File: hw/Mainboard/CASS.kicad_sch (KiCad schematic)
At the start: 16 parts, among them J5 CASS A, J6 CASS B, Q1 AO3401A, Q3 AO3401A

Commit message: Document schematics
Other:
- note added: "Solder jumpers allow cassette ports A/B to be configured as device 1 or 2. This is to support the original chicklet PETs where the internal cassette port is device 1 for use with the built-in Datasette. From schematics, MOTOR voltage appears to be 6.1V @ 350ma max per port. Datasettes uses a centrifugal speed governor, so voltage is not critical. +5V is rated 100ma per Datasette port. LED provide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"
- note removed: "+5V is 100ma per Datasette MOTOR is 6.1V @ 350ma max (older C2Ns draw more) SWITCH: 5v = Not pressed, Gnd = Pressed MOTOR: 5v = Off, Gnd = On (PIA1, pin 19)"
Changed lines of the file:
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@@
     (stroke (width 0) (type default) (color 0 0 0 0))
   )
-  (text "+5V is 100ma per Datasette\nMOTOR is 6.1V @ 350ma max (older C2Ns draw more)\n\nSWITCH: 5v = Not pressed, Gnd = Pressed\nMOTOR: 5v = Off, Gnd = On (PIA1, pin 19)\n"
-    (at 190.5 46.99 0)
+  (text "Solder jumpers allow cassette ports A/B to be configured as device 1 or 2.\nThis is to support the original chicklet PETs where the internal cassette\nport is device 1 for use with the built-in Datasette.\n\nFrom schematics, MOTOR voltage appears to be 6.1V @ 350ma max per port.\nDatasettes uses a centrifugal speed governor, so voltage is not critical.\n+5V is rated 100ma per Datasette port.\n\nLED provides an ~2V drop.  This accounts for the difference between the\n5V CMOS logic and the +6V input, causing the P-Channel MOSFET to turn off\ncompletely when ~{MOTOR} is high.  It also avoids over-voltaging the PIA.\n"
+    (at 190.5 57.15 0)
     (effects (font (size 1.27 1.27)) (justify left bottom))
   )
@@
   )
   (symbol (lib_id "power:+6V") (at 214.63 114.3 0) (unit 1)
-    (in_bom yes) (on_board yes) (fields_autoplaced)
+    (in_bom yes) (on_board yes)
     (property "Reference" "#PWR0125" (id 0) (at 214.63 118.11 0)
       (effects (font (size 1.27 1.27)) hide)
     )
-    (property "Value" "+6V" (id 1) (at 214.63 108.585 0))
+    (property "Value" "+6V" (id 1) (at 214.63 109.855 0))
     (property "Footprint" "" (id 2) (at 214.63 114.3 0)
       (effects (font (size 1.27 1.27)) hide)
@@
   )
   (symbol (lib_id "power:+6V") (at 214.63 82.55 0) (unit 1)
-    (in_bom yes) (on_board yes) (fields_autoplaced)
+    (in_bom yes) (on_board yes)
     (property "Reference" "#PWR0135" (id 0) (at 214.63 86.36 0)
       (effects (font (size 1.27 1.27)) hide)
     )
-    (property "Value" "+6V" (id 1) (at 214.63 76.835 0))
+    (property "Value" "+6V" (id 1) (at 214.63 78.105 0))
     (property "Footprint" "" (id 2) (at 214.63 82.55 0)
       (effects (font (size 1.27 1.27)) hide)

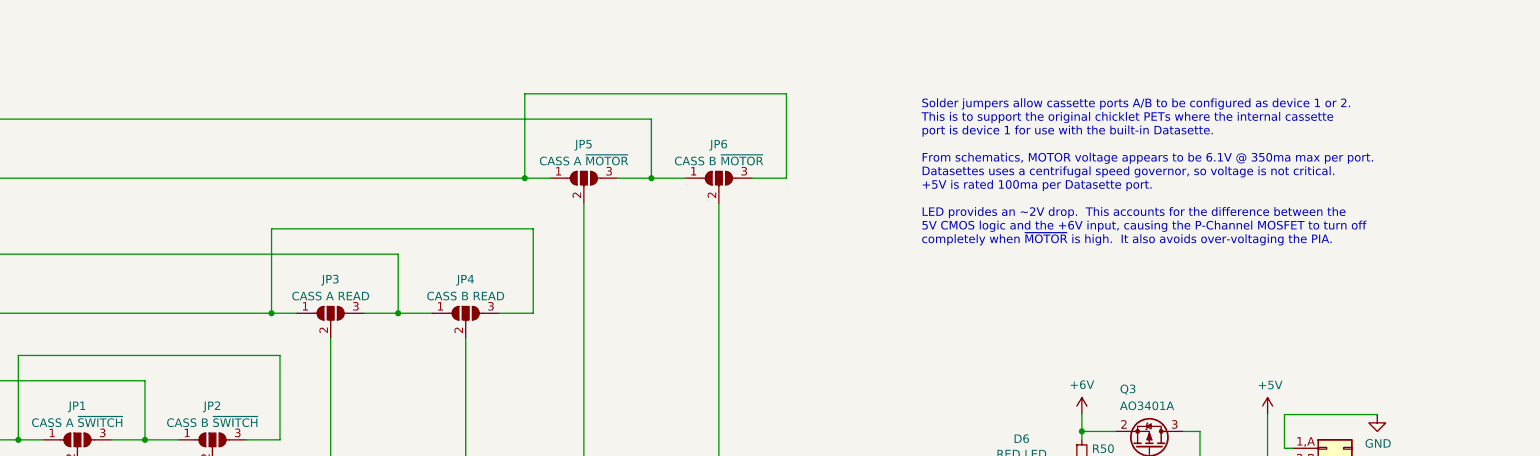
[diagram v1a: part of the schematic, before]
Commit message: hw: more schematic comments / cleanup
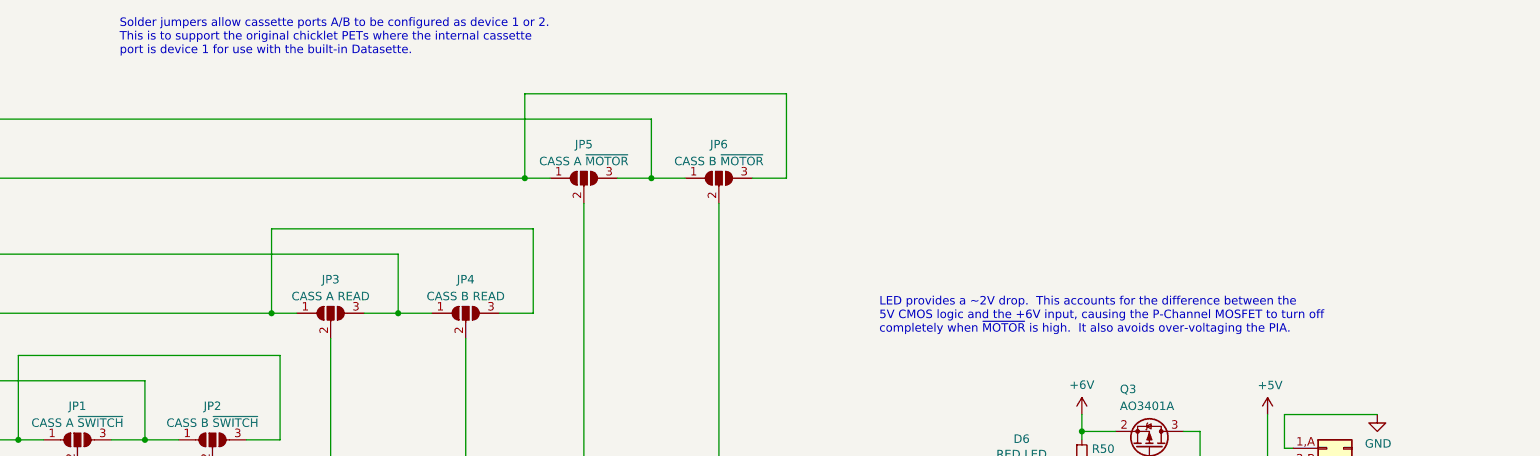
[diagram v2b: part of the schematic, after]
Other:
- note added: "LED provides a ~2V drop. This accounts for the difference between the 5V CMOS logic and the +6V input, causing the P-Channel MOSFET to turn off completely when ~{MOTOR} is high. It also avoids over-voltaging the PIA."
- note added: "Solder jumpers allow cassette ports A/B to be configured as device 1 or 2. This is to support the original chicklet PETs where the internal cassette port is device 1 for use with the built-in Datasette."
- note removed: "Solder jumpers allow cassette ports A/B to be configured as device 1 or 2. This is to support the original chicklet PETs where the internal cassette port is device 1 for use with the built-in Datasette. From schematics, MOTOR voltage appears to be 6.1V @ 350ma max per port. Datasettes uses a centrifugal speed governor, so voltage is not critical. +5V is rated 100ma per Datasette port. LED provide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"
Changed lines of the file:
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@@
     (stroke (width 0) (type default) (color 0 0 0 0))
   )
-  (text "Solder jumpers allow cassette ports A/B to be configured as device 1 or 2.\nThis is to support the original chicklet PETs where the internal cassette\nport is device 1 for use with the built-in Datasette.\n\nFrom schematics, MOTOR voltage appears to be 6.1V @ 350ma max per port.\nDatasettes uses a centrifugal speed governor, so voltage is not critical.\n+5V is rated 100ma per Datasette port.\n\nLED provides an ~2V drop.  This accounts for the difference between the\n5V CMOS logic and the +6V input, causing the P-Channel MOSFET to turn off\ncompletely when ~{MOTOR} is high.  It also avoids over-voltaging the PIA.\n"
-    (at 190.5 57.15 0)
+  (text "Solder jumpers allow cassette ports A/B to be configured as device 1 or 2.\nThis is to support the original chicklet PETs where the internal cassette\nport is device 1 for use with the built-in Datasette.\n"
+    (at 69.85 28.575 0)
     (effects (font (size 1.27 1.27)) (justify left bottom))
   )
+  (text "LED provides a ~2V drop.  This accounts for the difference between the\n5V CMOS logic and the +6V input, causing the P-Channel MOSFET to turn off\ncompletely when ~{MOTOR} is high.  It also avoids over-voltaging the PIA."
+    (at 184.15 70.485 0)
+    (effects (font (size 1.27 1.27)) (justify left bottom))
+  )

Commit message: hw: wip add MCU, 2 layer board
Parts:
- J5, J6: footprint PET:EDGE_CON_12P_TAPE -> Retrocomputing:CBM_PET_CASS_EDGE_CON_12P; symbol Mainboard-rescue:Conn_01x06_Card_Edge-PET -> Retrocomputing:CBM_PET_CASS_Conn_01x06_Card_Edge
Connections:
- net CASS_B_MOTOR: now reaches J6.3,C (MOTOR), Q1.3 (D)
- net CASS_A_MOTOR: now reaches J5.3,C (MOTOR), Q3.3 (D)
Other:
- moved on the sheet: D6, D7, Q1, Q3, R44, R50

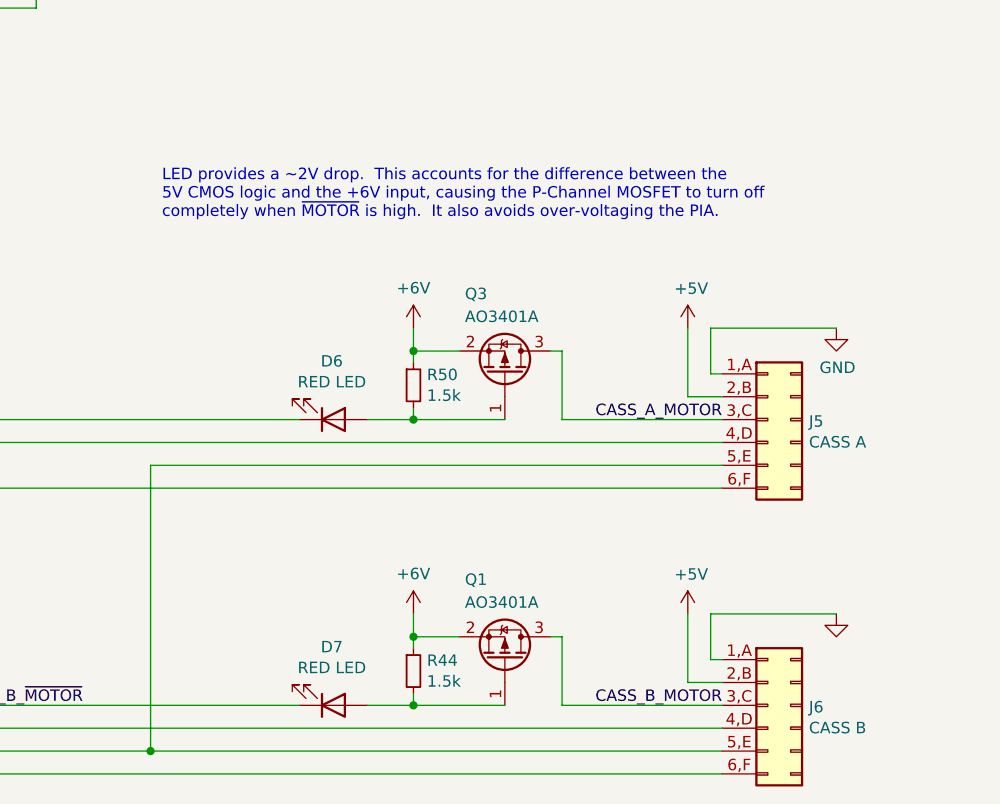
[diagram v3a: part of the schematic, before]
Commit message: hw: routed, but trace sizes need to be reviewed/fixed
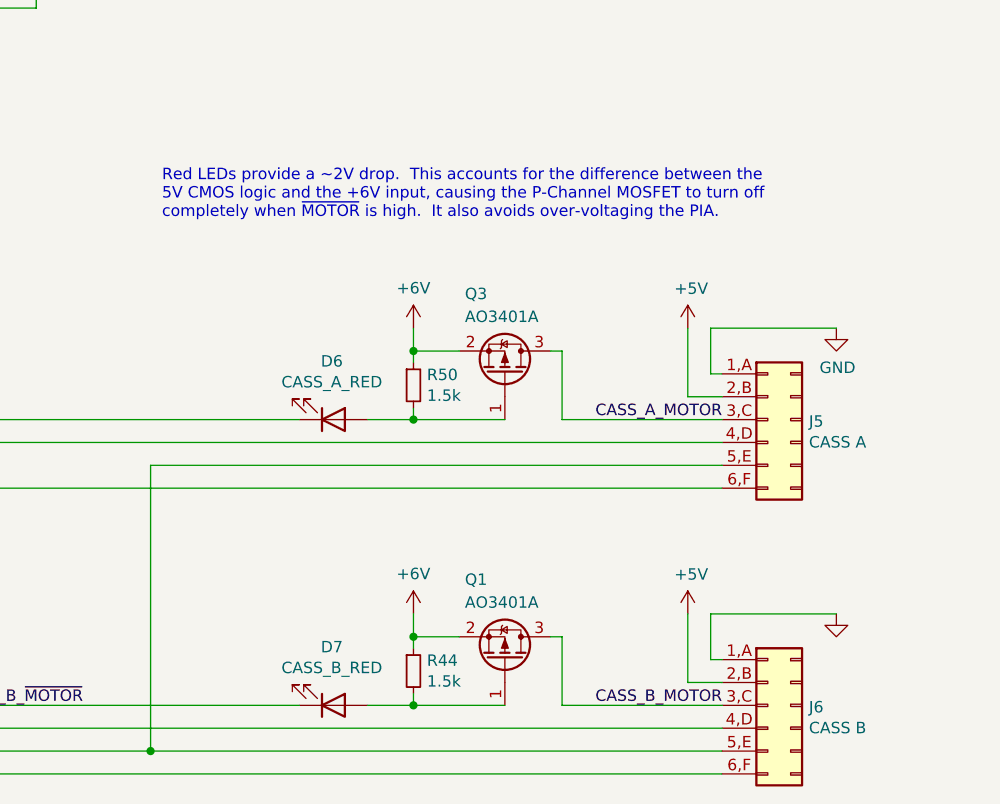
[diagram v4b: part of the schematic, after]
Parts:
- D6: value RED LED -> CASS_A_RED
- D7: value RED LED -> CASS_B_RED
- Q1, Q3: footprint PET:SOT-23-3L -> JLCPCB:SOT-23_L2.9-W1.3-P1.90-LS2.4-BR
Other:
- note added: "Red LEDs provide a ~2V drop. This accounts for the difference between the 5V CMOS logic and the +6V input, causing the P-Channel MOSFET to turn off completely when ~{MOTOR} is high. It also avoids over-voltaging the PIA."
- note removed: "LED provides a ~2V drop. This accounts for the difference between the 5V CMOS logic and the +6V input, causing the P-Channel MOSFET to turn off completely when ~{MOTOR} is high. It also avoids over-voltaging the PIA."
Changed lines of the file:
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@@
     (effects (font (size 1.27 1.27)) (justify left bottom))
   )
-  (text "LED provides a ~2V drop.  This accounts for the difference between the\n5V CMOS logic and the +6V input, causing the P-Channel MOSFET to turn off\ncompletely when ~{MOTOR} is high.  It also avoids over-voltaging the PIA."
+  (text "Red LEDs provide a ~2V drop.  This accounts for the difference between the\n5V CMOS logic and the +6V input, causing the P-Channel MOSFET to turn off\ncompletely when ~{MOTOR} is high.  It also avoids over-voltaging the PIA."
     (at 184.15 70.485 0)
     (effects (font (size 1.27 1.27)) (justify left bottom))
@@
       (effects (font (size 1.27 1.27)) (justify left))
     )
-    (property "Footprint" "PET:SOT-23-3L" (id 2) (at 220.345 82.55 0)
+    (property "Footprint" "JLCPCB:SOT-23_L2.9-W1.3-P1.90-LS2.4-BR" (id 2) (at 220.345 82.55 0)
       (effects (font (size 1.27 1.27) italic) (justify left) hide)
     )
@@
       (effects (font (size 1.27 1.27)) (justify left))
     )
-    (property "Footprint" "PET:SOT-23-3L" (id 2) (at 220.345 114.3 0)
+    (property "Footprint" "JLCPCB:SOT-23_L2.9-W1.3-P1.90-LS2.4-BR" (id 2) (at 220.345 114.3 0)
       (effects (font (size 1.27 1.27) italic) (justify left) hide)
     )
@@
     (in_bom yes) (on_board yes)
     (property "Reference" "D6" (id 0) (at 203.0222 86.233 0))
-    (property "Value" "RED LED" (id 1) (at 203.0222 88.5444 0))
+    (property "Value" "CASS_A_RED" (id 1) (at 203.0222 88.5444 0))
     (property "Footprint" "LED_SMD:LED_0603_1608Metric" (id 2) (at 203.2 92.71 0)
       (effects (font (size 1.27 1.27)) hide)
@@
     (in_bom yes) (on_board yes)
     (property "Reference" "D7" (id 0) (at 203.0222 117.983 0))
-    (property "Value" "RED LED" (id 1) (at 203.0222 120.2944 0))
+    (property "Value" "CASS_B_RED" (id 1) (at 203.0222 120.2944 0))
     (property "Footprint" "LED_SMD:LED_0603_1608Metric" (id 2) (at 203.2 124.46 0)
       (effects (font (size 1.27 1.27)) hide)

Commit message: hw: routable (wip)
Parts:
- added NT11, NT12: +6V, PET:NetTie-2_SMD_Pad_1.6_to_0.4mm, symbol Device:NetTie_2
- R44, R50: value 1.5k -> 1k5
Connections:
- net +5V: no longer J5.2,B (+5V), J6.2,B (+5V)
- net +6V renamed PD_6V
- net PD_6V: now also NT11.1, NT12.1; no longer R44.1, R50.1
- net GND renamed PD_GND
- new net: NT12.2, R50.1
- new net: NT11.2, R44.1
- new net PD_5V: J5.2,B (+5V), J6.2,B (+5V)
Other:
- moved on the sheet: D6, D7, R44, R50

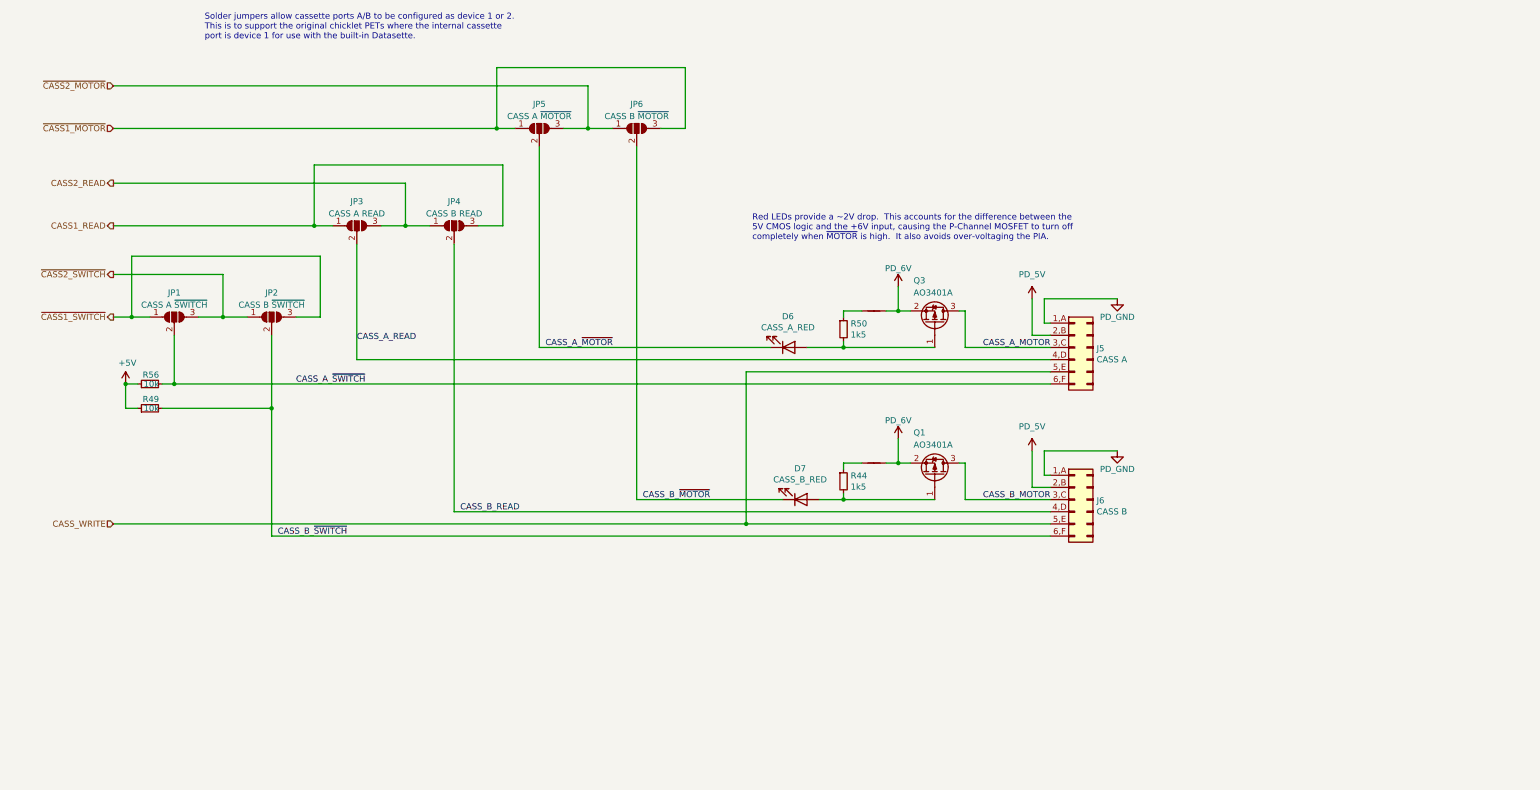
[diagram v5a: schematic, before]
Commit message: hw: larger schematic pages, routed w/netties
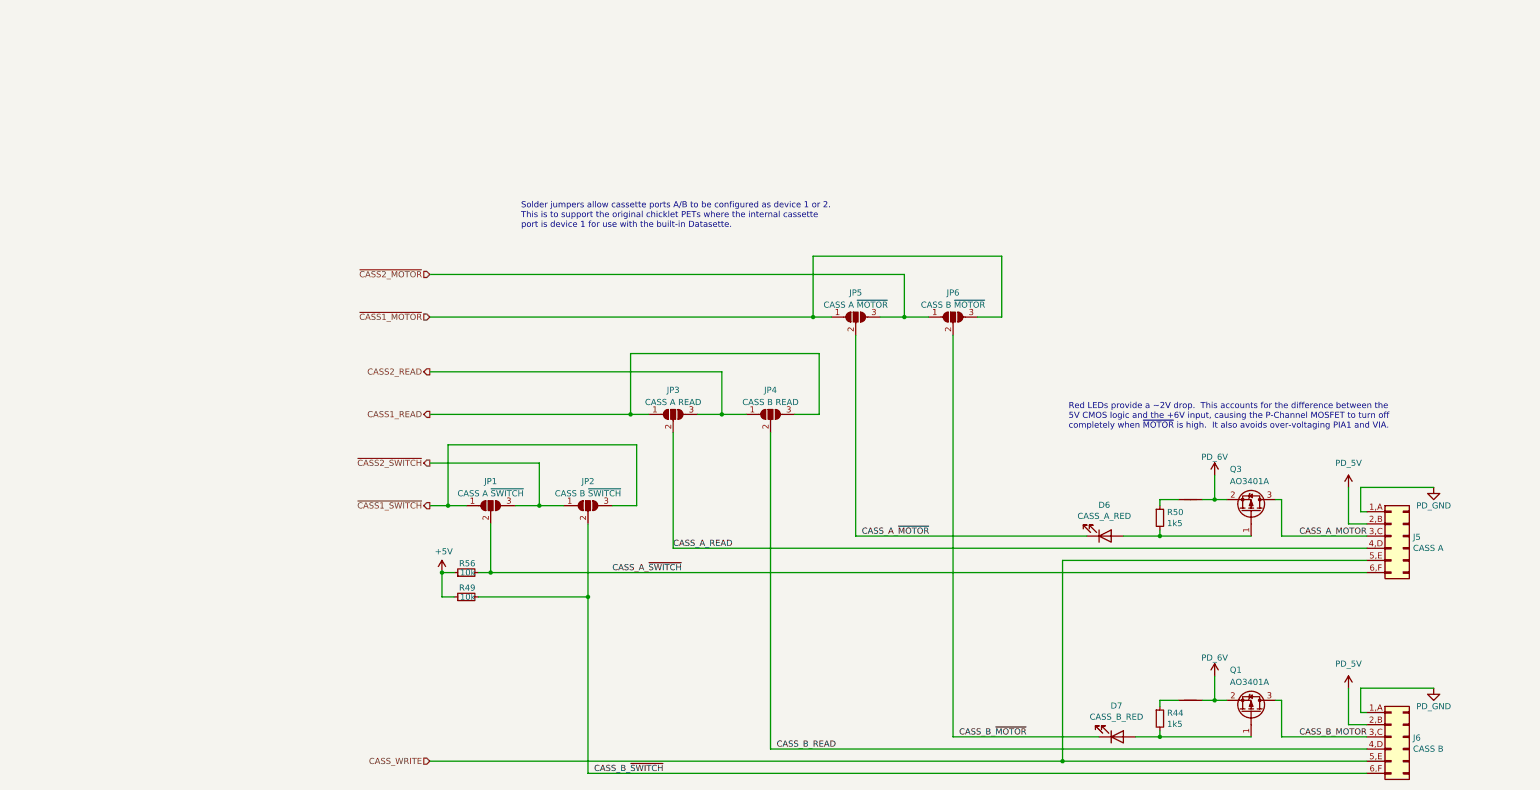
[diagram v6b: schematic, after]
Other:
- note added: "Red LEDs provide a ~2V drop. This accounts for the difference between the 5V CMOS logic and the +6V input, causing the P-Channel MOSFET to turn off completely when ~{MOTOR} is high. It also avoids over-voltaging PIA1 and VIA."
- note removed: "Red LEDs provide a ~2V drop. This accounts for the difference between the 5V CMOS logic and the +6V input, causing the P-Channel MOSFET to turn off completely when ~{MOTOR} is high. It also avoids over-voltaging the PIA."
- moved on the sheet: D6, D7, J5, J6, JP1, JP2, JP3, JP4, JP5, JP6, Q1, Q3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
